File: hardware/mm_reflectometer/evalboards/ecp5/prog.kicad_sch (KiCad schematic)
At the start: 87 parts, among them J301 USB_C_Receptacle_USB2.0, J302 JTAG, J303 Flash, J304 USB_C_Receptacle_USB2.0, U101 ECP5U_25_CABGA256, U301 93LC56C, U302 TPD3S014, U303 FT2232HQ, U304 TPD3S014, U305 W25Q32JVSS, X301 ASE-xxxMHz, Y301 7M-12.000MAAJ

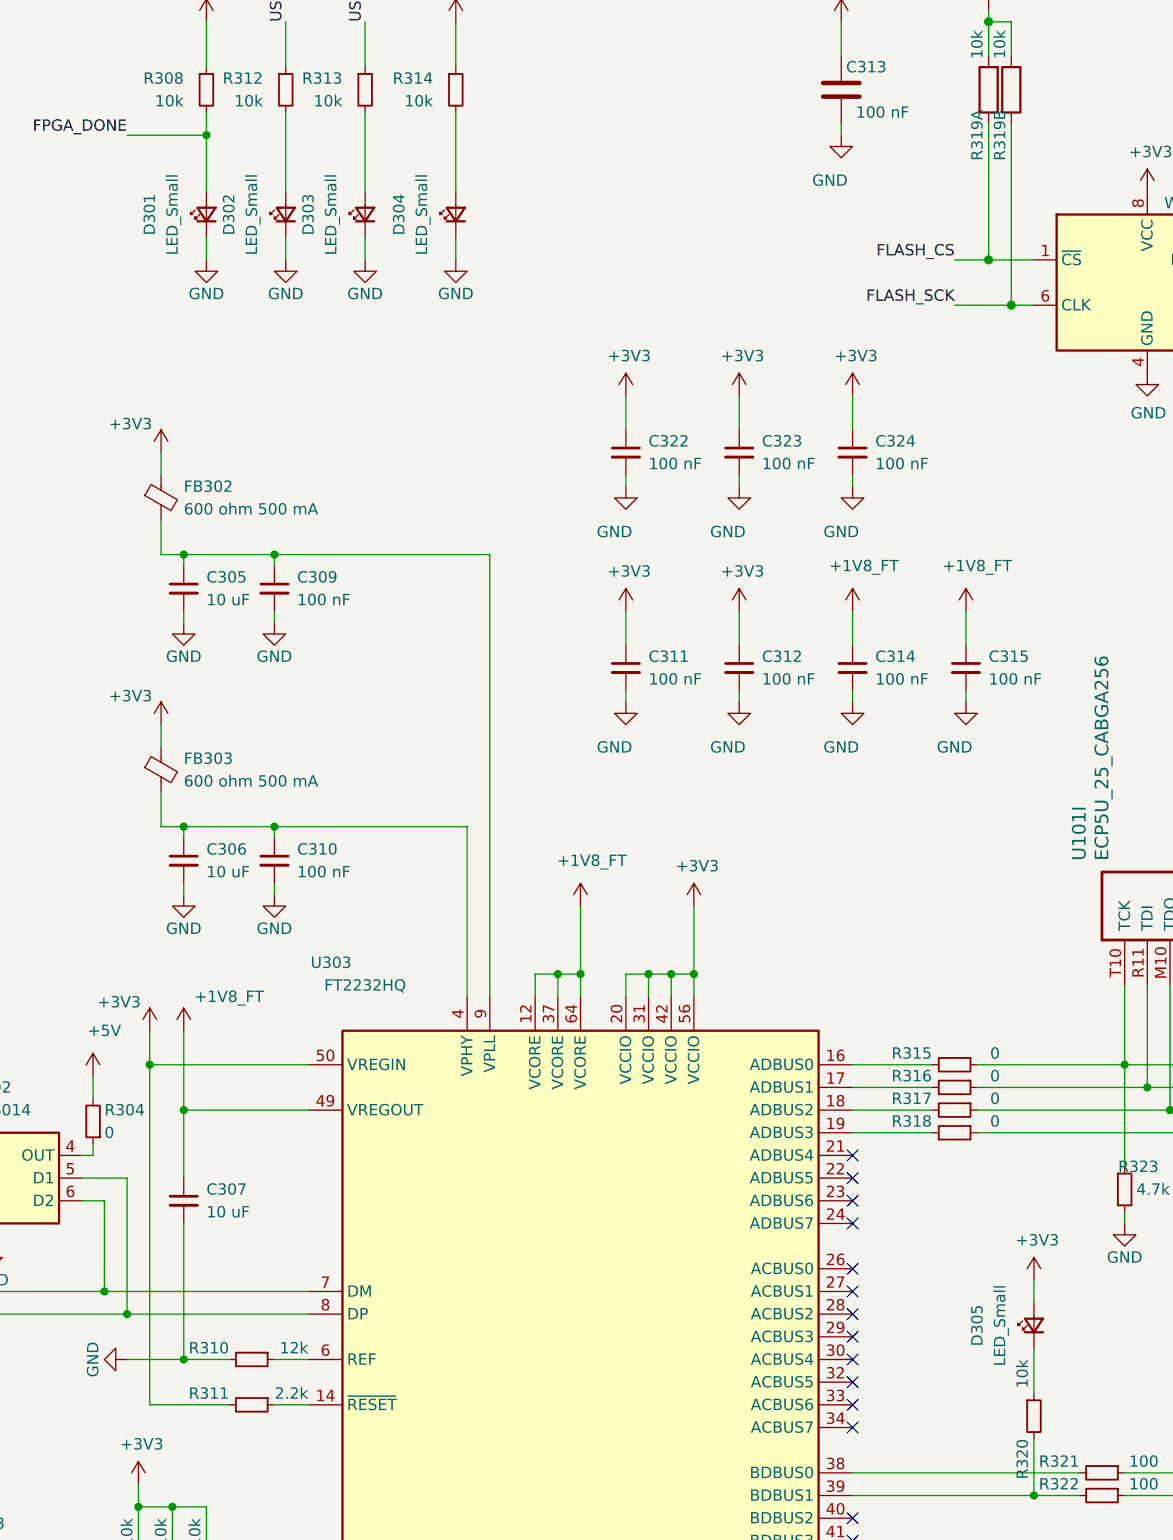
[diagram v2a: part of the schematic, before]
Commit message: cleanup ecp5 schematic, generated assembly drawings
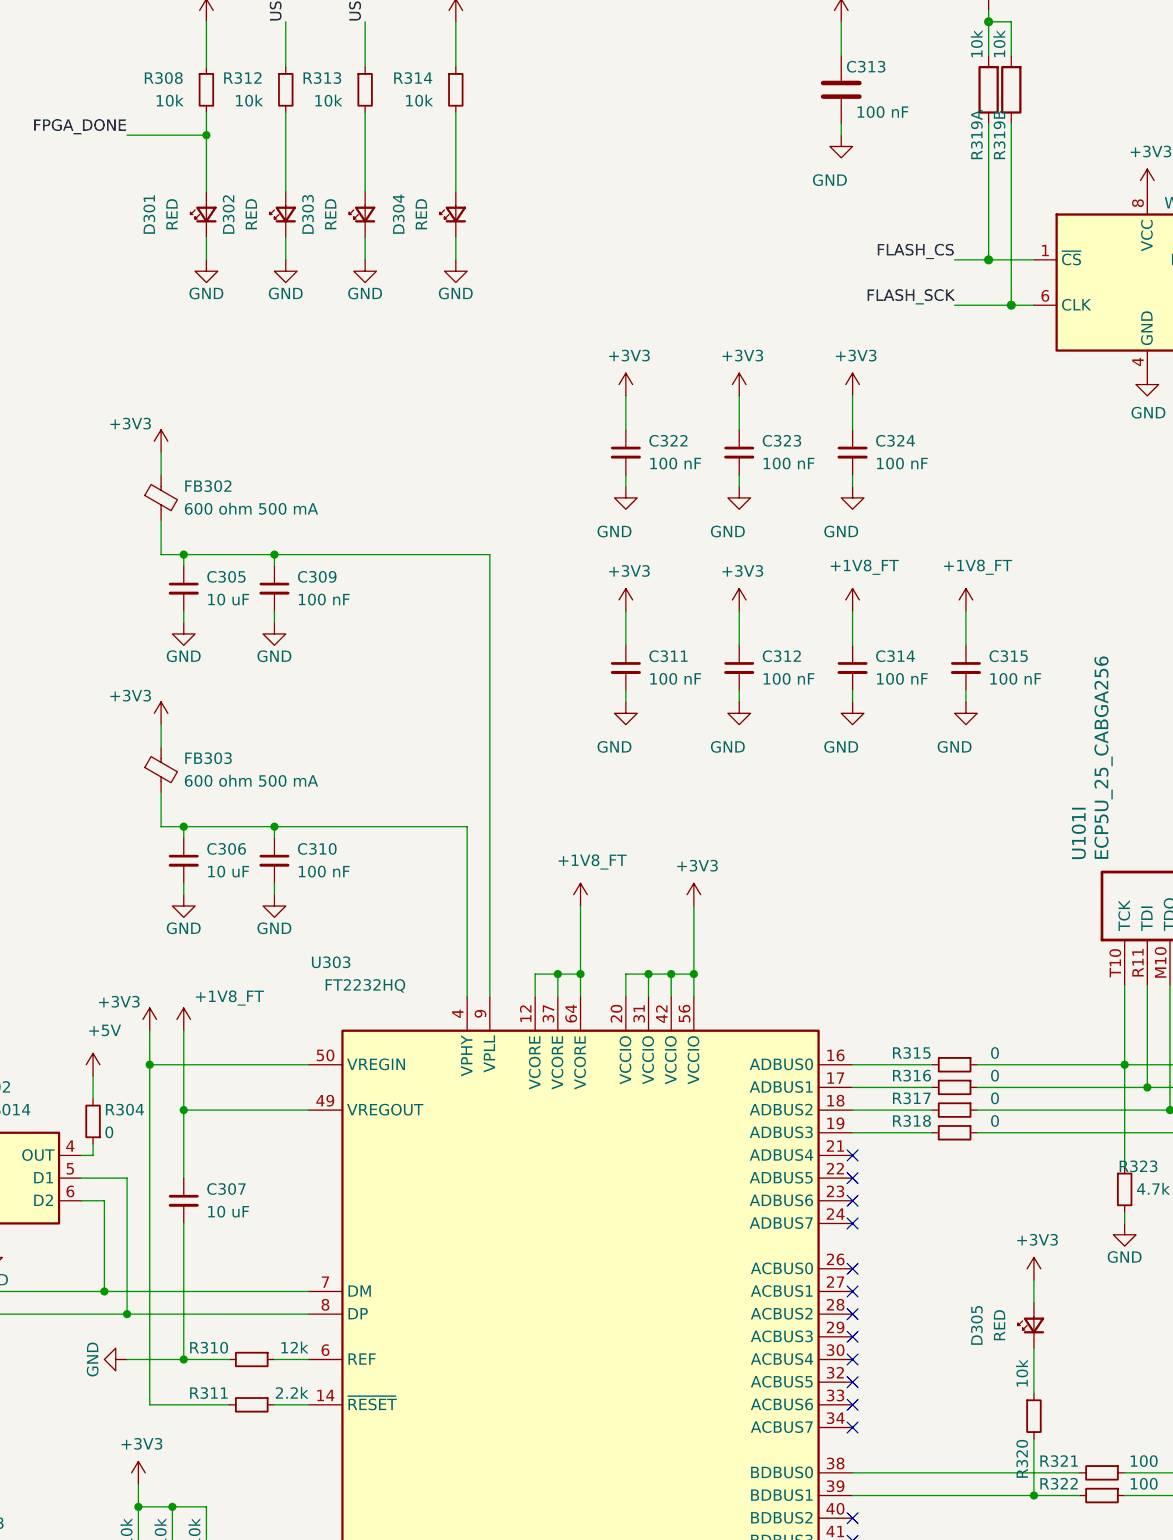
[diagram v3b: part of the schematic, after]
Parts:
- D301, D302, D303, D304, D305: value LED_Small -> RED
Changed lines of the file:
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@@
   (junction (at 370.84 24.13) (diameter 0.9144) (color 0 0 0 0))
   (junction (at 393.7 154.94) (diameter 0.9144) (color 0 0 0 0))
-  (no_connect (at 176.53 163.83))
-  (no_connect (at 176.53 186.69))
-  (no_connect (at 176.53 204.47))
-  (no_connect (at 176.53 207.01))
-  (no_connect (at 176.53 184.15))
-  (no_connect (at 176.53 179.07))
-  (no_connect (at 176.53 214.63))
-  (no_connect (at 57.15 191.77))
   (no_connect (at 176.53 176.53))
-  (no_connect (at 176.53 234.95))
+  (no_connect (at 176.53 207.01))
+  (no_connect (at 176.53 163.83))
+  (no_connect (at 176.53 245.11))
   (no_connect (at 243.84 254))
   (no_connect (at 176.53 229.87))
-  (no_connect (at 176.53 245.11))
-  (no_connect (at 176.53 181.61))
-  (no_connect (at 176.53 240.03))
-  (no_connect (at 176.53 232.41))
-  (no_connect (at 176.53 247.65))
-  (no_connect (at 176.53 212.09))
-  (no_connect (at 176.53 227.33))
-  (no_connect (at 176.53 166.37))
-  (no_connect (at 176.53 237.49))
+  (no_connect (at 176.53 171.45))
+  (no_connect (at 176.53 222.25))
+  (no_connect (at 57.15 191.77))
   (no_connect (at 57.15 194.31))
   (no_connect (at 176.53 217.17))
   (no_connect (at 243.84 251.46))
-  (no_connect (at 176.53 171.45))
+  (no_connect (at 176.53 179.07))
+  (no_connect (at 176.53 227.33))
   (no_connect (at 176.53 224.79))
-  (no_connect (at 176.53 194.31))
-  (no_connect (at 176.53 209.55))
-  (no_connect (at 176.53 189.23))
-  (no_connect (at 176.53 222.25))
-  (no_connect (at 176.53 191.77))
+  (no_connect (at 176.53 240.03))
   (no_connect (at 176.53 168.91))
+  (no_connect (at 176.53 232.41))
+  (no_connect (at 176.53 166.37))
+  (no_connect (at 176.53 191.77))
+  (no_connect (at 176.53 186.69))
+  (no_connect (at 176.53 189.23))
+  (no_connect (at 176.53 209.55))
+  (no_connect (at 176.53 184.15))
+  (no_connect (at 176.53 237.49))
+  (no_connect (at 176.53 247.65))
+  (no_connect (at 176.53 212.09))
+  (no_connect (at 176.53 194.31))
+  (no_connect (at 176.53 214.63))
+  (no_connect (at 176.53 181.61))
+  (no_connect (at 176.53 234.95))
+  (no_connect (at 176.53 204.47))
   (wire (pts (xy 16.51 205.74) (xy 16.51 208.28))
     (stroke (width 0) (type solid) (color 0 0 0 0))
@@
     (in_bom yes) (on_board yes)
     (property "Reference" "D301" (id 0) (at 97.79 58.42 0))
-    (property "Value" "LED_Small" (id 1) (at 100.33 58.42 0))
+    (property "Value" "RED" (id 1) (at 100.33 58.42 0))
     (property "Footprint" "LED_SMD:LED_0603_1608Metric" (id 2) (at 104.14 58.42 90)
       (effects (font (size 1.27 1.27)) hide)
@@
     (in_bom yes) (on_board yes)
     (property "Reference" "D302" (id 0) (at 106.68 58.42 0))
-    (property "Value" "LED_Small" (id 1) (at 109.22 58.42 0))
+    (property "Value" "RED" (id 1) (at 109.22 58.42 0))
     (property "Footprint" "LED_SMD:LED_0603_1608Metric" (id 2) (at 113.03 58.42 90)
       (effects (font (size 1.27 1.27)) hide)
@@
     (in_bom yes) (on_board yes)
     (property "Reference" "D303" (id 0) (at 115.57 58.42 0))
-    (property "Value" "LED_Small" (id 1) (at 118.11 58.42 0))
+    (property "Value" "RED" (id 1) (at 118.11 58.42 0))
     (property "Footprint" "LED_SMD:LED_0603_1608Metric" (id 2) (at 121.92 58.42 90)
       (effects (font (size 1.27 1.27)) hide)
@@
     (in_bom yes) (on_board yes)
     (property "Reference" "D304" (id 0) (at 125.73 58.42 0))
-    (property "Value" "LED_Small" (id 1) (at 128.27 58.42 0))
+    (property "Value" "RED" (id 1) (at 128.27 58.42 0))
     (property "Footprint" "LED_SMD:LED_0603_1608Metric" (id 2) (at 132.08 58.42 90)
       (effects (font (size 1.27 1.27)) hide)
@@
     (in_bom yes) (on_board yes)
     (property "Reference" "D305" (id 0) (at 190.5 182.88 0))
-    (property "Value" "LED_Small" (id 1) (at 193.04 182.88 0))
+    (property "Value" "RED" (id 1) (at 193.04 182.88 0))
     (property "Footprint" "LED_SMD:LED_0603_1608Metric" (id 2) (at 196.85 182.88 90)
       (effects (font (size 1.27 1.27)) hide)

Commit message: added support for hyperram and programming to flash to litex soc
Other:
- note added: "TODO: ADD RESET.."
- note added: "TODO: fix eeprom footprint, should be narrow SOIC"
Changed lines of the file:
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@@
     (effects (font (size 1.27 1.27)) (justify right bottom))
+  )
+  (text "TODO: fix eeprom footprint, should be narrow SOIC" (at 92.71 233.68 180)
+    (effects (font (size 3 3) (thickness 0.6) bold) (justify right bottom))
   )
   (text "Flash and sequencer schematic and symbol adapted from Greg Davill's ECPBreaker\nCC-BY-SA V4.0"
@@
     (effects (font (size 1.27 1.27)) (justify left bottom))
   )
+  (text "TODO: ADD RESET.." (at 391.16 181.61 180)
+    (effects (font (size 3 3) (thickness 0.6) bold) (justify right bottom))
+  )
   (label "FT_EECS" (at 66.04 222.25 180)
